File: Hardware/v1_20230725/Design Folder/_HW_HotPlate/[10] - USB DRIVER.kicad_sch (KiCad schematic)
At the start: 7 parts, among them J1001 MICRO B USB_RA, U1001 DLPT05A-7, U1002 DLPT05A-7

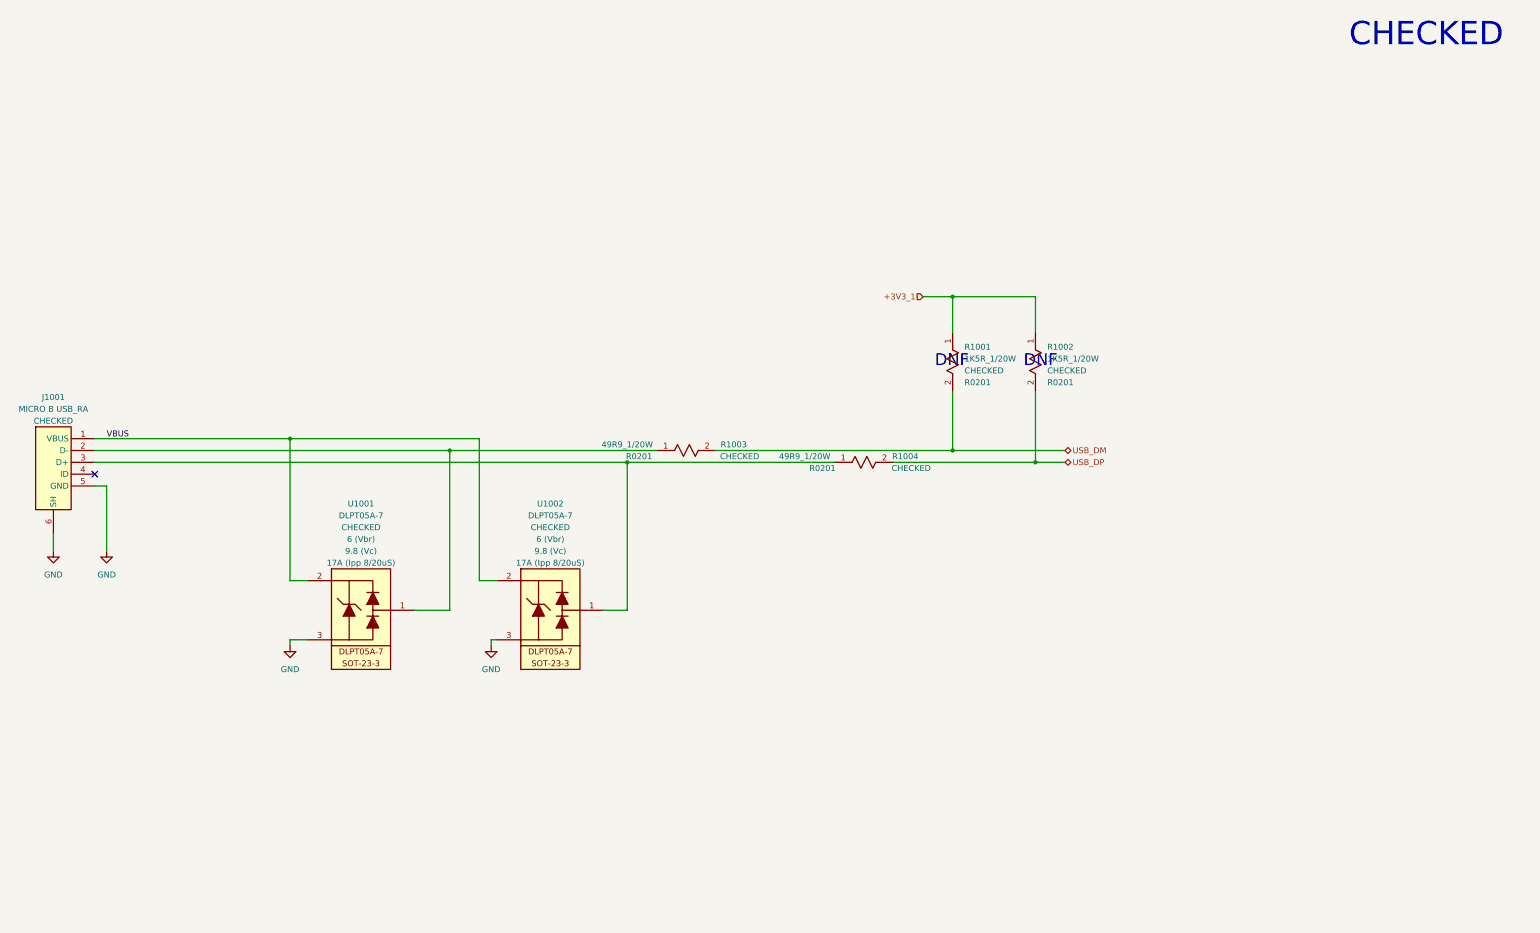
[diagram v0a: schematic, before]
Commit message: Schematic library has been updated
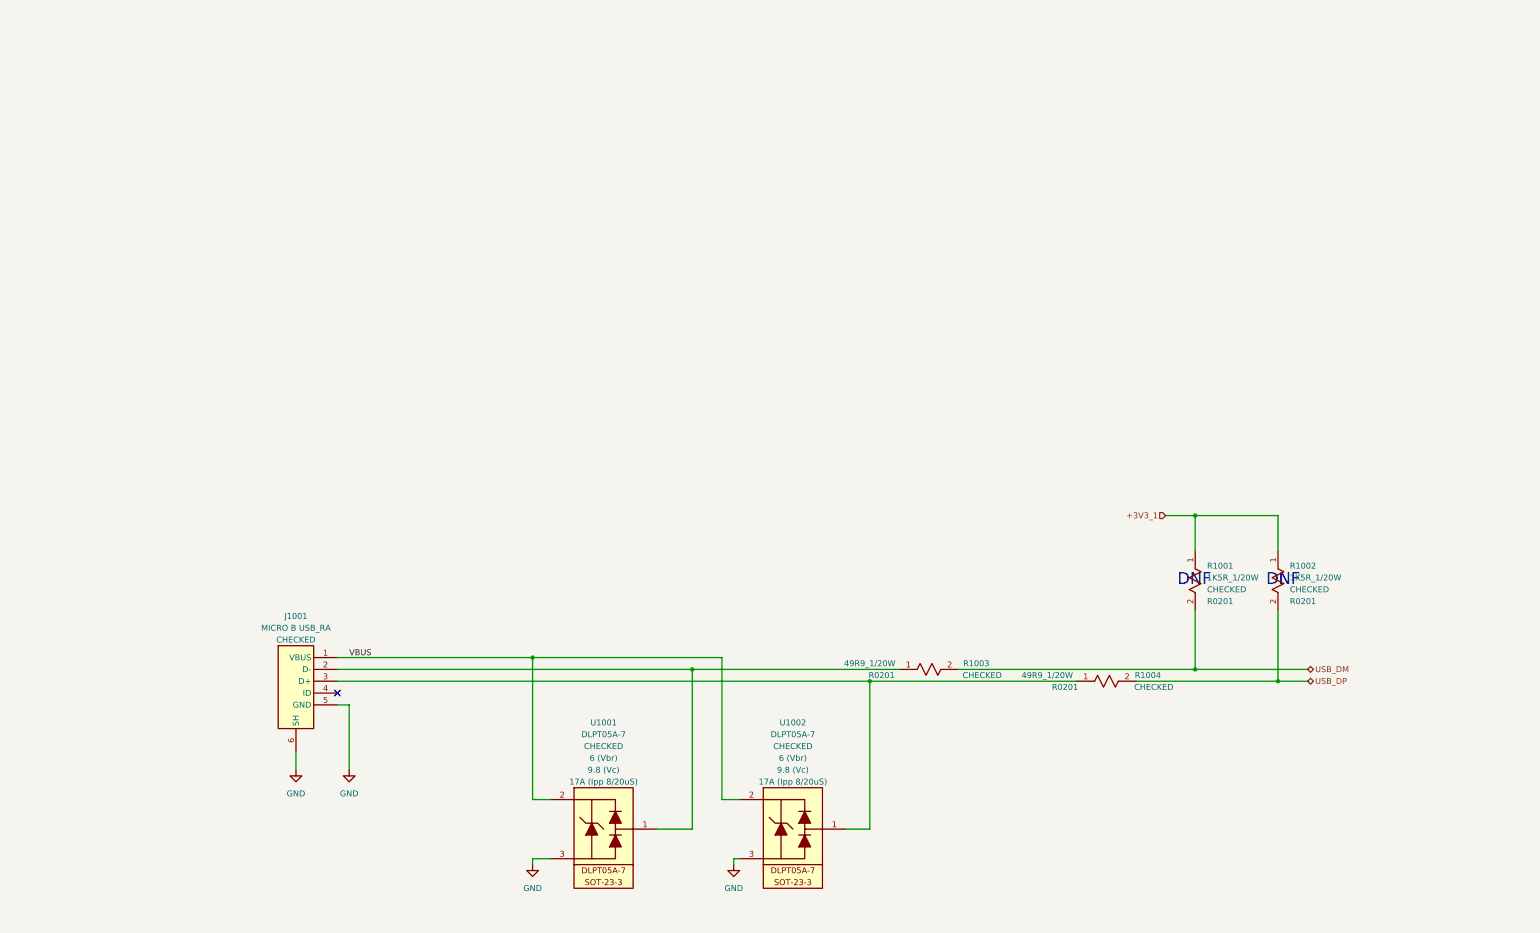
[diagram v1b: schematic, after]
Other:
- note removed: "CHECKED"
- moved on the sheet: J1001, R1001, R1002, R1003, R1004, U1001, U1002

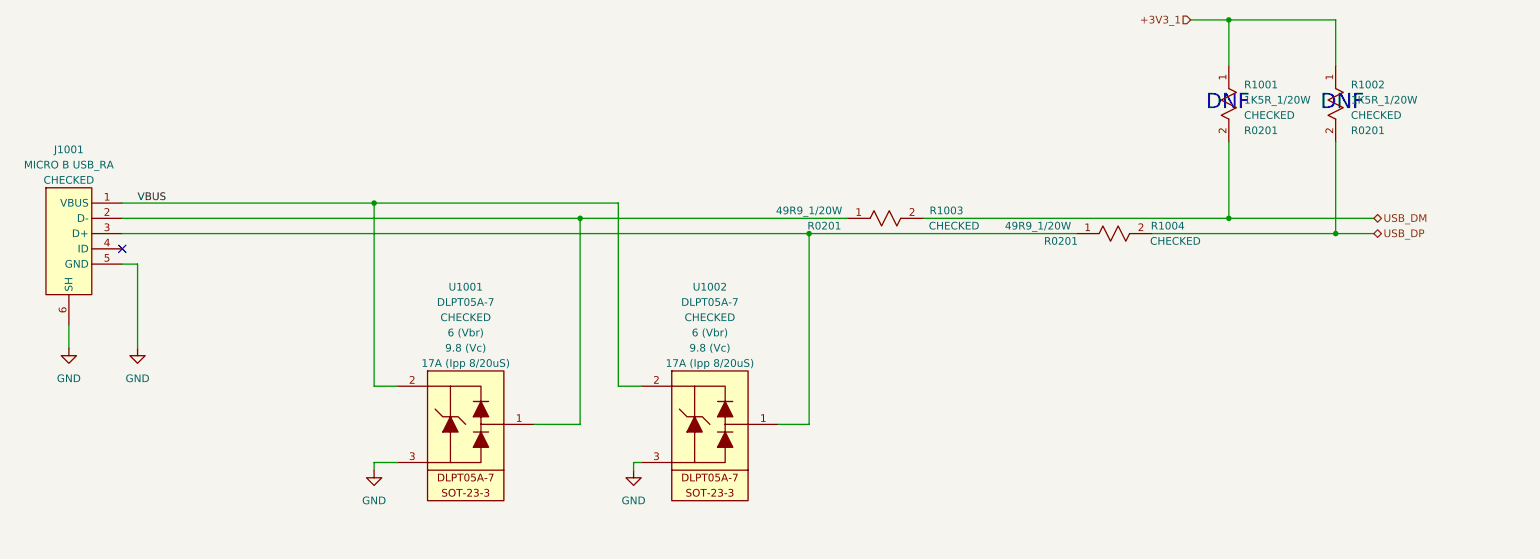
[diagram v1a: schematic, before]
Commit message: components have been updated
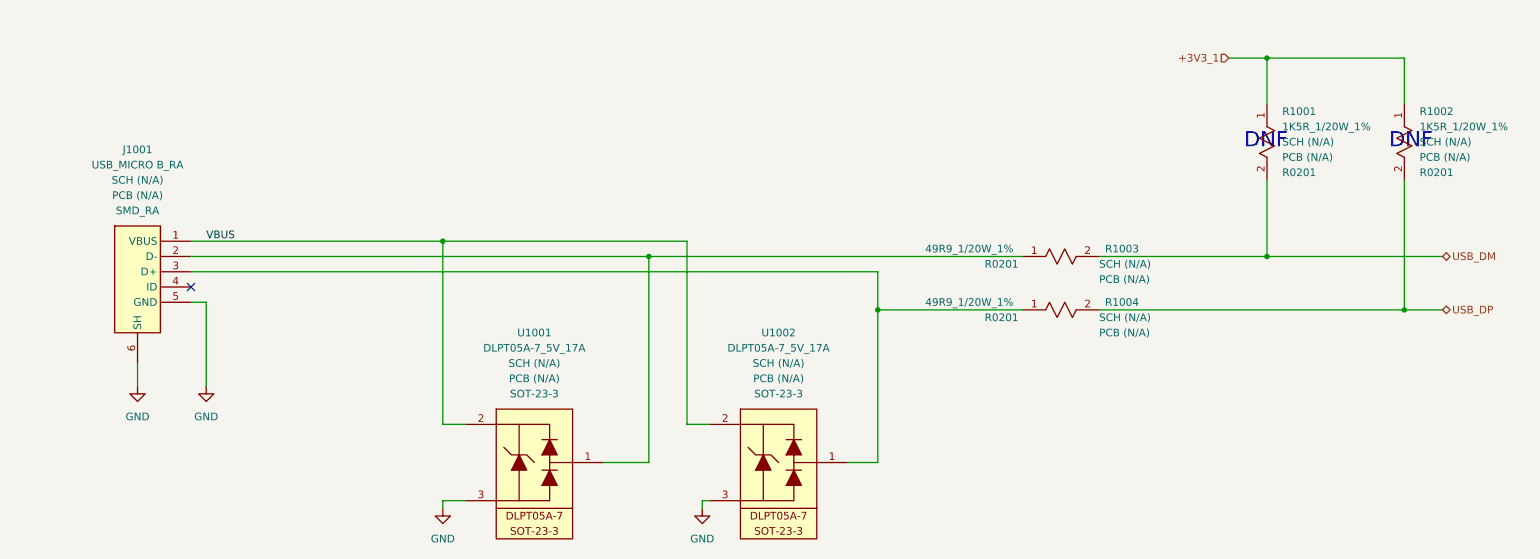
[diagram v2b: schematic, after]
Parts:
- J1001: value MICRO B USB_RA -> USB_MICRO B_RA; symbol _SCHLIB_HotPlate:CONN_USB MICRO B-10118194-0001LF -> _SCHLIB_HotPlate:CONN_USB MICRO B-10118194-0001LF_5POS_RA_SMD; Manufacturer (none) -> Amphenol ICC (FCI); PCB CHECk (none) -> PCB (N/A); Package (none) -> SMD_RA; Part Number 10118194-0001LF -> (none); Part Number (Manufacturer) (none) -> 10118194-0001LF; Part Number (Vendor) (none) -> 609-4618-2-ND; SCH CHECK CHECKED -> SCH (N/A); Vendor (none) -> Digikey
- R1001, R1002: value 1K5R_1/20W -> 1K5R_1/20W_1%; symbol _SCHLIB_HotPlate:RES_1K5R_1/20W_R0201 -> _SCHLIB_HotPlate:RES_1K5R_1/20W_1%_R0201; Manufacturer (none) -> YAGEO; PCB CHECk (none) -> PCB (N/A); Part Number RC0201FR-071K4L -> (none); Part Number (Manufacturer) (none) -> RC0201FR-071K4L; Part Number (Vendor) (none) -> YAG2483TR-ND; SCH CHECK CHECKED -> SCH (N/A); Vendor (none) -> Digikey
- R1003, R1004: value 49R9_1/20W -> 49R9_1/20W_1%; symbol _SCHLIB_HotPlate:RES_49R9_1/20W-R0201 -> _SCHLIB_HotPlate:RES_49R9_1/20W_1%_R0201; Manufacturer (none) -> Stackpole Electronics Inc; PCB CHECk (none) -> PCB (N/A); Part Number RMCF0201FT49R9 -> (none); Part Number (Manufacturer) (none) -> RMCF0201FT49R9; Part Number (Vendor) (none) -> RMCF0201FT49R9TR-ND; SCH CHECK CHECKED -> SCH (N/A); Vendor (none) -> Digikey
- U1001, U1002: value DLPT05A-7 -> DLPT05A-7_5V_17A; symbol _SCHLIB_HotPlate:TVS_DLPT05A-7_SOT_23 -> _SCHLIB_HotPlate:DIODE_TVS_DLPT05A-7_5V_6V_17A(8/20us)_SOT_23; Ipp 17A (Ipp 8/20uS) -> (none); Manufacturer (none) -> Diodes Incorporated; PCB CHECk (none) -> PCB (N/A); Package (none) -> SOT-23-3; Part Number DLPT05A-7 -> (none); Part Number (Manufacturer) (none) -> DLPT05A-7; Part Number (Vendor) (none) -> 31-DLPT05A-7TR-ND; SCH CHECK CHECKED -> SCH (N/A); Vbr 6 (Vbr) -> (none); Vc 9.8 (Vc) -> (none); Vendor (none) -> Digikey
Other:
- moved on the sheet: J1001, R1001, R1002, R1003, R1004, U1001, U1002

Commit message: Updating hardware format structure
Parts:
- J1001: footprint Connector_USB:USB_Micro-B_Amphenol_10118194_Horizontal -> _PCBLIB_HotPlate:USB_Micro-B_Amphenol_10118194_Horizontal
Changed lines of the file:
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@@
       (effects (font (size 1.27 1.27)))
     )
-    (property "Footprint" "Connector_USB:USB_Micro-B_Amphenol_10118194_Horizontal" (at 165.1 154.94 0)
+    (property "Footprint" "_PCBLIB_HotPlate:USB_Micro-B_Amphenol_10118194_Horizontal" (at 165.1 154.94 0)
       (effects (font (size 1.27 1.27)) (justify left) hide)
     )
